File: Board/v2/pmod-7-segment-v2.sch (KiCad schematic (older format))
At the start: 17 parts, among them J1 PMOD

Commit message: v2 updates
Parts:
- J1: symbol pmod-7-segment-v2-rescue:PMOD -> pmod-7-segment-v2-rescue:PMOD-pmod-7-segment-v2-rescue
- LED1, LED2, LED3, LED4, LED5, LED6, LED7, LED8: symbol pmod-7-segment-v2-rescue:SA39-11 -> pmod-7-segment-v2-rescue:SA39-11-pmod-7-segment-v2-rescue
- R1, R2, R3, R4, R5, R6, R7, R8: symbol pmod-7-segment-v2-rescue:R -> pmod-7-segment-v2-rescue:R-pmod-7-segment-v2-rescue
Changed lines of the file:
@@
 $EndDescr
 $Comp
-L pmod-7-segment-v2-rescue:SA39-11 LED1
+L pmod-7-segment-v2-rescue:SA39-11-pmod-7-segment-v2-rescue LED1
 U 1 1 54A80DD5
 P 3300 2050
@@
 $EndComp
 $Comp
-L pmod-7-segment-v2-rescue:SA39-11 LED2
+L pmod-7-segment-v2-rescue:SA39-11-pmod-7-segment-v2-rescue LED2
 U 1 1 54A80DFF
 P 4700 2050
@@
 $EndComp
 $Comp
-L pmod-7-segment-v2-rescue:SA39-11 LED3
+L pmod-7-segment-v2-rescue:SA39-11-pmod-7-segment-v2-rescue LED3
 U 1 1 54A80E2A
 P 6100 2050
@@
 $EndComp
 $Comp
-L pmod-7-segment-v2-rescue:SA39-11 LED4
+L pmod-7-segment-v2-rescue:SA39-11-pmod-7-segment-v2-rescue LED4
 U 1 1 54A80E55
 P 7500 2050
@@
 $EndComp
 $Comp
-L pmod-7-segment-v2-rescue:SA39-11 LED5
+L pmod-7-segment-v2-rescue:SA39-11-pmod-7-segment-v2-rescue LED5
 U 1 1 54A80E7B
 P 3300 3450
@@
 $EndComp
 $Comp
-L pmod-7-segment-v2-rescue:SA39-11 LED6
+L pmod-7-segment-v2-rescue:SA39-11-pmod-7-segment-v2-rescue LED6
 U 1 1 54A80E9E
 P 4700 3450
@@
 $EndComp
 $Comp
-L pmod-7-segment-v2-rescue:SA39-11 LED7
+L pmod-7-segment-v2-rescue:SA39-11-pmod-7-segment-v2-rescue LED7
 U 1 1 54A80EC5
 P 6100 3450
@@
 $EndComp
 $Comp
-L pmod-7-segment-v2-rescue:SA39-11 LED8
+L pmod-7-segment-v2-rescue:SA39-11-pmod-7-segment-v2-rescue LED8
 U 1 1 54A80EF3
 P 7500 3450
@@
 NoConn ~ 10400 2750
 $Comp
-L pmod-7-segment-v2-rescue:R R1
+L pmod-7-segment-v2-rescue:R-pmod-7-segment-v2-rescue R1
 U 1 1 54A81B67
 P 2550 4900
@@
 $EndComp
 $Comp
-L pmod-7-segment-v2-rescue:R R2
+L pmod-7-segment-v2-rescue:R-pmod-7-segment-v2-rescue R2
 U 1 1 54A81BA6
 P 2550 5000
@@
 $EndComp
 $Comp
-L pmod-7-segment-v2-rescue:R R3
+L pmod-7-segment-v2-rescue:R-pmod-7-segment-v2-rescue R3
 U 1 1 54A81BEE
 P 2550 5100
@@
 $EndComp
 $Comp
-L pmod-7-segment-v2-rescue:R R4
+L pmod-7-segment-v2-rescue:R-pmod-7-segment-v2-rescue R4
 U 1 1 54A81C31
 P 2550 5200
@@
 $EndComp
 $Comp
-L pmod-7-segment-v2-rescue:R R5
+L pmod-7-segment-v2-rescue:R-pmod-7-segment-v2-rescue R5
 U 1 1 54A81C73
 P 3950 4900
@@
 $EndComp
 $Comp
-L pmod-7-segment-v2-rescue:R R6
+L pmod-7-segment-v2-rescue:R-pmod-7-segment-v2-rescue R6
 U 1 1 54A81CBF
 P 3950 5000
@@
 $EndComp
 $Comp
-L pmod-7-segment-v2-rescue:R R7
+L pmod-7-segment-v2-rescue:R-pmod-7-segment-v2-rescue R7
 U 1 1 54A81D0A
 P 3950 5100
@@
 $EndComp
 $Comp
-L pmod-7-segment-v2-rescue:R R8
+L pmod-7-segment-v2-rescue:R-pmod-7-segment-v2-rescue R8
 U 1 1 54A81D58
 P 3950 5200
@@
 $EndComp
 $Comp
-L pmod-7-segment-v2-rescue:GND #PWR?
+L pmod-7-segment-v2-rescue:GND-pmod-7-segment-v2-rescue #PWR?
 U 1 1 54A82B4B
 P 2800 5300
@@
 $EndComp
 $Comp
-L pmod-7-segment-v2-rescue:GND #PWR?
+L pmod-7-segment-v2-rescue:GND-pmod-7-segment-v2-rescue #PWR?
 U 1 1 54A82B70
 P 3700 5300
@@
 $EndComp
 $Comp
-L pmod-7-segment-v2-rescue:PMOD J1
+L pmod-7-segment-v2-rescue:PMOD-pmod-7-segment-v2-rescue J1
 U 1 1 54A828DA
 P 3250 5150

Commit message: v2.0 routed and DRC ok, ready for mfg
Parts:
- J1: symbol pmod-7-segment-v2-rescue:PMOD-pmod-7-segment-v2-rescue -> pmod-7-segment-v2-rescue:PMOD-pmod-7-segment-v2-rescue-pmod-7-segment-v2-rescue
- LED1, LED2, LED3, LED4, LED5, LED6, LED7, LED8: footprint Kingbright:SA39-11 -> pmod-7-segment-v2:10pcs-1bit-1-bit-Common-Anode-Positive-Digital-Tube-0-36-0-36in-Red-LED-Digit; symbol pmod-7-segment-v2-rescue:SA39-11-pmod-7-segment-v2-rescue -> pmod-7-segment-v2-rescue:SA39-11-pmod-7-segment-v2-rescue-pmod-7-segment-v2-rescue
- R1, R2, R3, R4, R5, R6, R7, R8: symbol pmod-7-segment-v2-rescue:R-pmod-7-segment-v2-rescue -> pmod-7-segment-v2-rescue:R-pmod-7-segment-v2-rescue-pmod-7-segment-v2-rescue
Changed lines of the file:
@@
 EESchema Schematic File Version 4
 LIBS:pmod-7-segment-v2-cache
-EELAYER 26 0
+EELAYER 29 0
 EELAYER END
 $Descr A4 11693 8268
@@
 $EndDescr
 $Comp
-L pmod-7-segment-v2-rescue:SA39-11-pmod-7-segment-v2-rescue LED1
+L pmod-7-segment-v2-rescue:SA39-11-pmod-7-segment-v2-rescue-pmod-7-segment-v2-rescue LED1
 U 1 1 54A80DD5
 P 3300 2050
 F 0 "LED1" H 3000 2550 60  0000 L CNN
 F 1 "SA39-11" H 3000 1550 60  0000 L CNN
-F 2 "Kingbright:SA39-11" H 3600 1700 60  0001 C CNN
+F 2 "pmod-7-segment-v2:10pcs-1bit-1-bit-Common-Anode-Positive-Digital-Tube-0-36-0-36in-Red-LED-Digit" H 3600 1700 60  0001 C CNN
 F 3 "" H 3600 1700 60  0000 C CNN
 	1    3300 2050
@@
 $EndComp
 $Comp
-L pmod-7-segment-v2-rescue:SA39-11-pmod-7-segment-v2-rescue LED2
+L pmod-7-segment-v2-rescue:SA39-11-pmod-7-segment-v2-rescue-pmod-7-segment-v2-rescue LED2
 U 1 1 54A80DFF
 P 4700 2050
 F 0 "LED2" H 4400 2550 60  0000 L CNN
 F 1 "SA39-11" H 4400 1550 60  0000 L CNN
-F 2 "Kingbright:SA39-11" H 5000 1700 60  0001 C CNN
+F 2 "pmod-7-segment-v2:10pcs-1bit-1-bit-Common-Anode-Positive-Digital-Tube-0-36-0-36in-Red-LED-Digit" H 5000 1700 60  0001 C CNN
 F 3 "" H 5000 1700 60  0000 C CNN
 	1    4700 2050
@@
 $EndComp
 $Comp
-L pmod-7-segment-v2-rescue:SA39-11-pmod-7-segment-v2-rescue LED3
+L pmod-7-segment-v2-rescue:SA39-11-pmod-7-segment-v2-rescue-pmod-7-segment-v2-rescue LED3
 U 1 1 54A80E2A
 P 6100 2050
 F 0 "LED3" H 5800 2550 60  0000 L CNN
 F 1 "SA39-11" H 5800 1550 60  0000 L CNN
-F 2 "Kingbright:SA39-11" H 6400 1700 60  0001 C CNN
+F 2 "pmod-7-segment-v2:10pcs-1bit-1-bit-Common-Anode-Positive-Digital-Tube-0-36-0-36in-Red-LED-Digit" H 6400 1700 60  0001 C CNN
 F 3 "" H 6400 1700 60  0000 C CNN
 	1    6100 2050
@@
 $EndComp
 $Comp
-L pmod-7-segment-v2-rescue:SA39-11-pmod-7-segment-v2-rescue LED4
+L pmod-7-segment-v2-rescue:SA39-11-pmod-7-segment-v2-rescue-pmod-7-segment-v2-rescue LED4
 U 1 1 54A80E55
 P 7500 2050
 F 0 "LED4" H 7200 2550 60  0000 L CNN
 F 1 "SA39-11" H 7200 1550 60  0000 L CNN
-F 2 "Kingbright:SA39-11" H 7800 1700 60  0001 C CNN
+F 2 "pmod-7-segment-v2:10pcs-1bit-1-bit-Common-Anode-Positive-Digital-Tube-0-36-0-36in-Red-LED-Digit" H 7800 1700 60  0001 C CNN
 F 3 "" H 7800 1700 60  0000 C CNN
 	1    7500 2050
@@
 $EndComp
 $Comp
-L pmod-7-segment-v2-rescue:SA39-11-pmod-7-segment-v2-rescue LED5
+L pmod-7-segment-v2-rescue:SA39-11-pmod-7-segment-v2-rescue-pmod-7-segment-v2-rescue LED5
 U 1 1 54A80E7B
 P 3300 3450
 F 0 "LED5" H 3000 3950 60  0000 L CNN
 F 1 "SA39-11" H 3000 2950 60  0000 L CNN
-F 2 "Kingbright:SA39-11" H 3600 3100 60  0001 C CNN
+F 2 "pmod-7-segment-v2:10pcs-1bit-1-bit-Common-Anode-Positive-Digital-Tube-0-36-0-36in-Red-LED-Digit" H 3600 3100 60  0001 C CNN
 F 3 "" H 3600 3100 60  0000 C CNN
 	1    3300 3450
@@
 $EndComp
 $Comp
-L pmod-7-segment-v2-rescue:SA39-11-pmod-7-segment-v2-rescue LED6
+L pmod-7-segment-v2-rescue:SA39-11-pmod-7-segment-v2-rescue-pmod-7-segment-v2-rescue LED6
 U 1 1 54A80E9E
 P 4700 3450
 F 0 "LED6" H 4400 3950 60  0000 L CNN
 F 1 "SA39-11" H 4400 2950 60  0000 L CNN
-F 2 "Kingbright:SA39-11" H 5000 3100 60  0001 C CNN
+F 2 "pmod-7-segment-v2:10pcs-1bit-1-bit-Common-Anode-Positive-Digital-Tube-0-36-0-36in-Red-LED-Digit" H 5000 3100 60  0001 C CNN
 F 3 "" H 5000 3100 60  0000 C CNN
 	1    4700 3450
@@
 $EndComp
 $Comp
-L pmod-7-segment-v2-rescue:SA39-11-pmod-7-segment-v2-rescue LED7
+L pmod-7-segment-v2-rescue:SA39-11-pmod-7-segment-v2-rescue-pmod-7-segment-v2-rescue LED7
 U 1 1 54A80EC5
 P 6100 3450
 F 0 "LED7" H 5800 3950 60  0000 L CNN
 F 1 "SA39-11" H 5800 2950 60  0000 L CNN
-F 2 "Kingbright:SA39-11" H 6400 3100 60  0001 C CNN
+F 2 "pmod-7-segment-v2:10pcs-1bit-1-bit-Common-Anode-Positive-Digital-Tube-0-36-0-36in-Red-LED-Digit" H 6400 3100 60  0001 C CNN
 F 3 "" H 6400 3100 60  0000 C CNN
 	1    6100 3450
@@
 $EndComp
 $Comp
-L pmod-7-segment-v2-rescue:SA39-11-pmod-7-segment-v2-rescue LED8
+L pmod-7-segment-v2-rescue:SA39-11-pmod-7-segment-v2-rescue-pmod-7-segment-v2-rescue LED8
 U 1 1 54A80EF3
 P 7500 3450
 F 0 "LED8" H 7200 3950 60  0000 L CNN
 F 1 "SA39-11" H 7200 2950 60  0000 L CNN
-F 2 "Kingbright:SA39-11" H 7800 3100 60  0001 C CNN
+F 2 "pmod-7-segment-v2:10pcs-1bit-1-bit-Common-Anode-Positive-Digital-Tube-0-36-0-36in-Red-LED-Digit" H 7800 3100 60  0001 C CNN
 F 3 "" H 7800 3100 60  0000 C CNN
 	1    7500 3450
@@
 NoConn ~ 10400 2750
 $Comp
-L pmod-7-segment-v2-rescue:R-pmod-7-segment-v2-rescue R1
+L pmod-7-segment-v2-rescue:R-pmod-7-segment-v2-rescue-pmod-7-segment-v2-rescue R1
 U 1 1 54A81B67
 P 2550 4900
@@
 $EndComp
 $Comp
-L pmod-7-segment-v2-rescue:R-pmod-7-segment-v2-rescue R2
+L pmod-7-segment-v2-rescue:R-pmod-7-segment-v2-rescue-pmod-7-segment-v2-rescue R2
 U 1 1 54A81BA6
 P 2550 5000
@@
 $EndComp
 $Comp
-L pmod-7-segment-v2-rescue:R-pmod-7-segment-v2-rescue R3
+L pmod-7-segment-v2-rescue:R-pmod-7-segment-v2-rescue-pmod-7-segment-v2-rescue R3
 U 1 1 54A81BEE
 P 2550 5100
@@
 $EndComp
 $Comp
-L pmod-7-segment-v2-rescue:R-pmod-7-segment-v2-rescue R4
+L pmod-7-segment-v2-rescue:R-pmod-7-segment-v2-rescue-pmod-7-segment-v2-rescue R4
 U 1 1 54A81C31
 P 2550 5200
@@
 $EndComp
 $Comp
-L pmod-7-segment-v2-rescue:R-pmod-7-segment-v2-rescue R5
+L pmod-7-segment-v2-rescue:R-pmod-7-segment-v2-rescue-pmod-7-segment-v2-rescue R5
 U 1 1 54A81C73
 P 3950 4900
@@
 $EndComp
 $Comp
-L pmod-7-segment-v2-rescue:R-pmod-7-segment-v2-rescue R6
+L pmod-7-segment-v2-rescue:R-pmod-7-segment-v2-rescue-pmod-7-segment-v2-rescue R6
 U 1 1 54A81CBF
 P 3950 5000
@@
 $EndComp
 $Comp
-L pmod-7-segment-v2-rescue:R-pmod-7-segment-v2-rescue R7
+L pmod-7-segment-v2-rescue:R-pmod-7-segment-v2-rescue-pmod-7-segment-v2-rescue R7
 U 1 1 54A81D0A
 P 3950 5100
@@
 $EndComp
 $Comp
-L pmod-7-segment-v2-rescue:R-pmod-7-segment-v2-rescue R8
+L pmod-7-segment-v2-rescue:R-pmod-7-segment-v2-rescue-pmod-7-segment-v2-rescue R8
 U 1 1 54A81D58
 P 3950 5200
@@
 $EndComp
 $Comp
-L pmod-7-segment-v2-rescue:GND-pmod-7-segment-v2-rescue #PWR?
+L pmod-7-segment-v2-rescue:GND-pmod-7-segment-v2-rescue-pmod-7-segment-v2-rescue #PWR?
 U 1 1 54A82B4B
 P 2800 5300
@@
 $EndComp
 $Comp
-L pmod-7-segment-v2-rescue:GND-pmod-7-segment-v2-rescue #PWR?
+L pmod-7-segment-v2-rescue:GND-pmod-7-segment-v2-rescue-pmod-7-segment-v2-rescue #PWR?
 U 1 1 54A82B70
 P 3700 5300
@@
 $EndComp
 $Comp
-L pmod-7-segment-v2-rescue:PMOD-pmod-7-segment-v2-rescue J1
+L pmod-7-segment-v2-rescue:PMOD-pmod-7-segment-v2-rescue-pmod-7-segment-v2-rescue J1
 U 1 1 54A828DA
 P 3250 5150

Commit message: pmod-7-segment-v2 : v2.1 as submitted to oshpark
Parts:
- LED1, LED2, LED3, LED4, LED5, LED6, LED7, LED8: symbol pmod-7-segment-v2-rescue:SA39-11-pmod-7-segment-v2-rescue-pmod-7-segment-v2-rescue -> tom-semiconductors:aliexpress-ca-7-segment-0.36in
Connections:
- net S0: now also LED8.1 (CA), LED8.6 (CA); no longer LED8.3 (CA), LED8.8 (CA)
- net S1: now also LED7.1 (CA), LED7.6 (CA); no longer LED7.3 (CA), LED7.8 (CA)
- net S2: now also LED1.8 (C), LED2.8 (C), LED3.8 (C), LED4.8 (C), LED5.8 (C), LED6.1 (CA), LED6.6 (CA); no longer LED1.7 (C), LED2.7 (C), LED3.7 (C), LED4.7 (C), LED5.7 (C), LED6.3 (CA), LED6.8 (CA)
- net S3: now also LED5.1 (CA), LED5.6 (CA), LED6.8 (C), LED7.8 (C), LED8.8 (C); no longer LED5.3 (CA), LED5.8 (CA), LED6.7 (C), LED7.7 (C), LED8.7 (C)
- net S4: now also LED4.1 (CA), LED4.6 (CA); no longer LED4.3 (CA), LED4.8 (CA)
- net S5: now also LED3.1 (CA), LED3.6 (CA); no longer LED3.3 (CA), LED3.8 (CA)
- net S6: now also LED1.3 (G), LED2.1 (CA), LED2.6 (CA); no longer LED1.1 (G), LED2.3 (CA), LED2.8 (CA)
- net S7: now also LED1.1 (CA), LED1.6 (CA), LED2.3 (G), LED3.3 (G), LED4.3 (G), LED5.3 (G), LED6.3 (G), LED7.3 (G), LED8.3 (G); no longer LED1.3 (CA), LED1.8 (CA), LED2.1 (G), LED3.1 (G), LED4.1 (G), LED5.1 (G), LED6.1 (G), LED7.1 (G), LED8.1 (G)

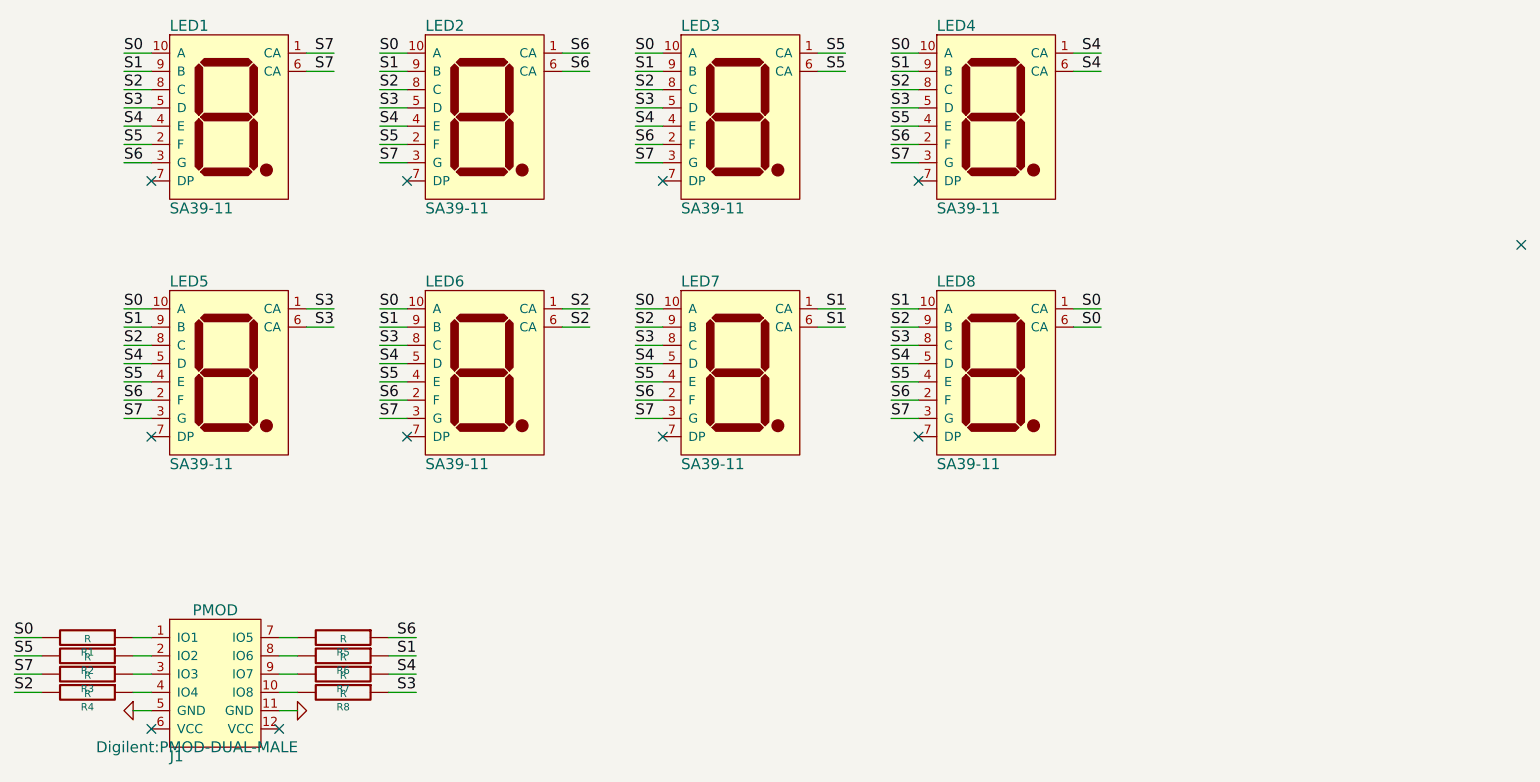
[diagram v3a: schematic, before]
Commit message: v2: renumber nets, fix SolderMaskClearance, fix copper pour isolation, v2.2
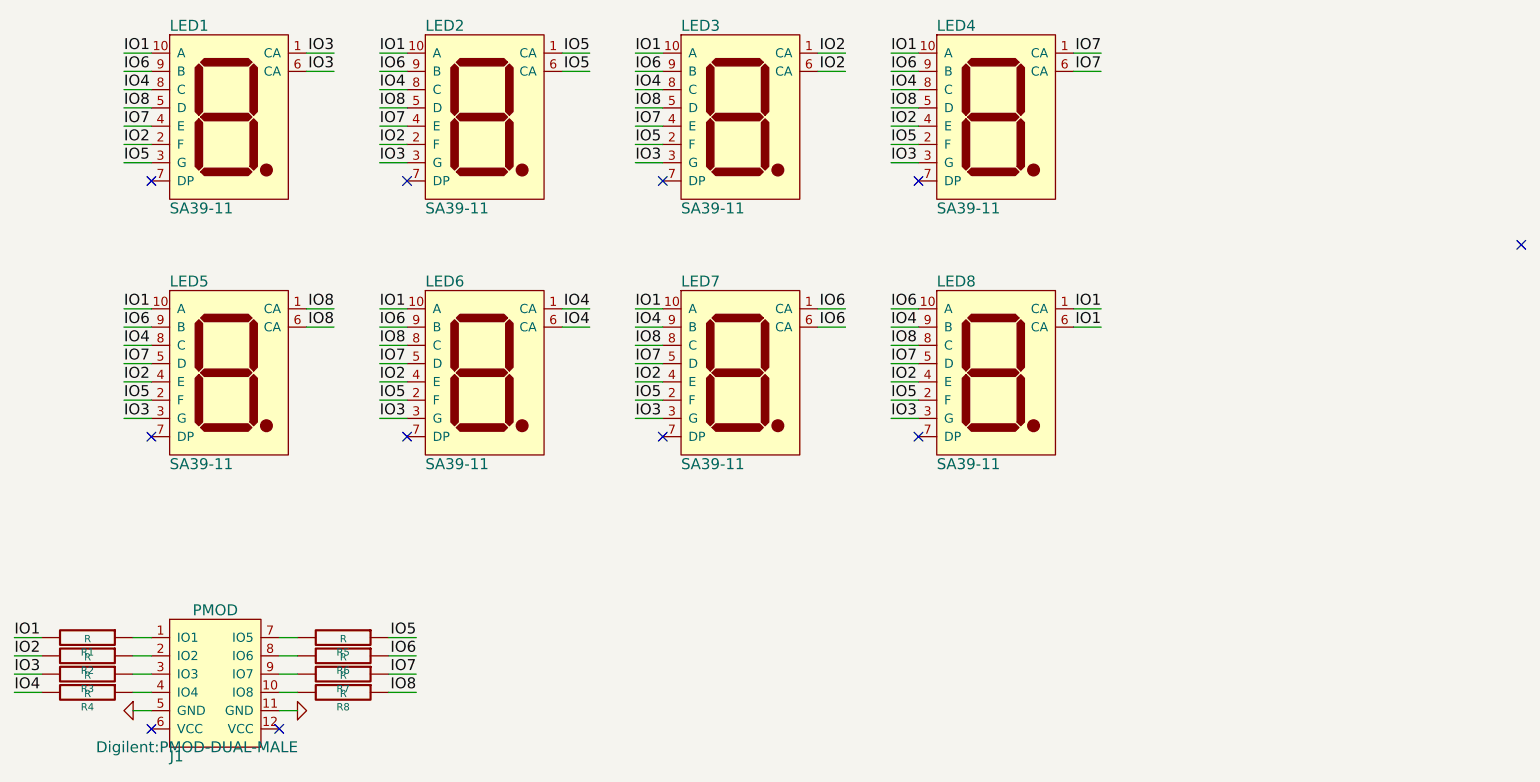
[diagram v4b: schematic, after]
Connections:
- net S0 renamed IO1
- net S1 renamed IO6
- net S2 renamed IO4
- net S3 renamed IO8
- net S4 renamed IO7
- net S5 renamed IO2
- net S6 renamed IO5
- net S7 renamed IO3
